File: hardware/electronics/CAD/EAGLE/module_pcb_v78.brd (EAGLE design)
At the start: 34.9 x 42.8 mm, 8 parts, among them J1 5557969-1

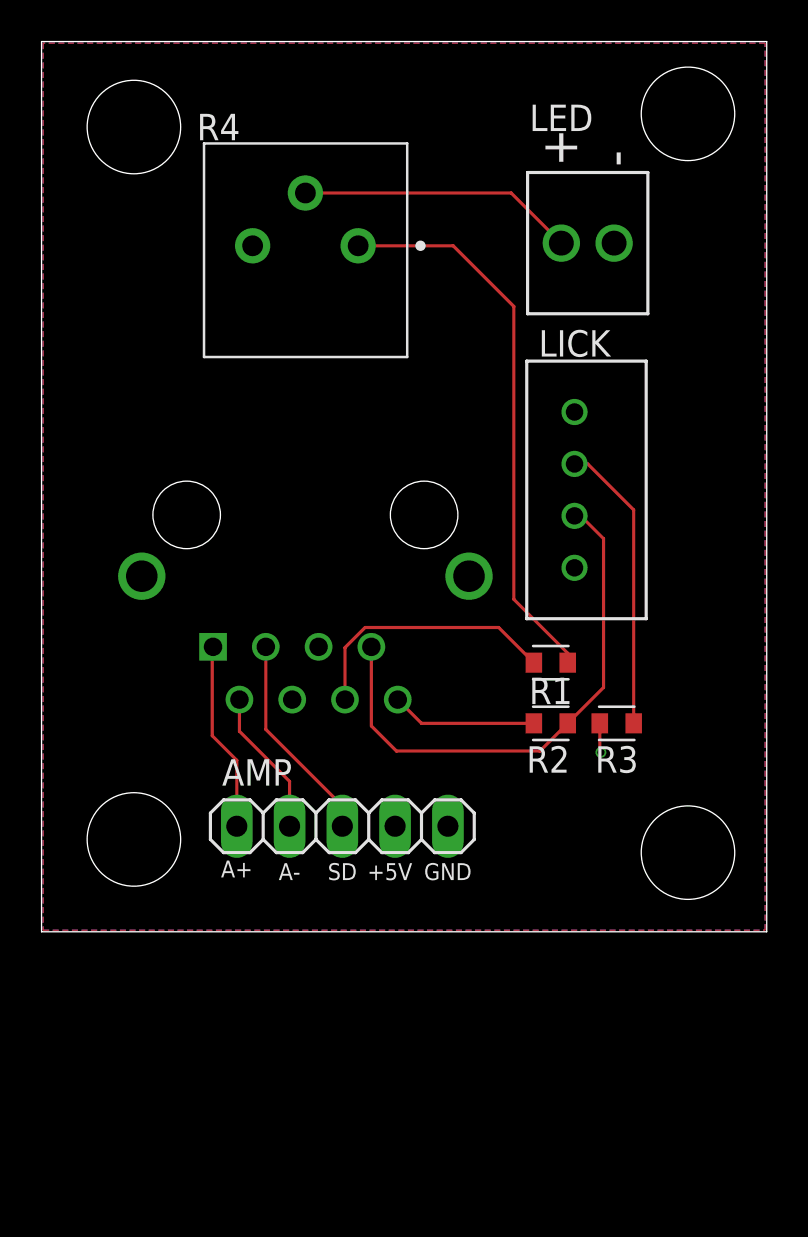
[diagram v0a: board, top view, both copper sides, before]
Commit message: round corners of module pcb
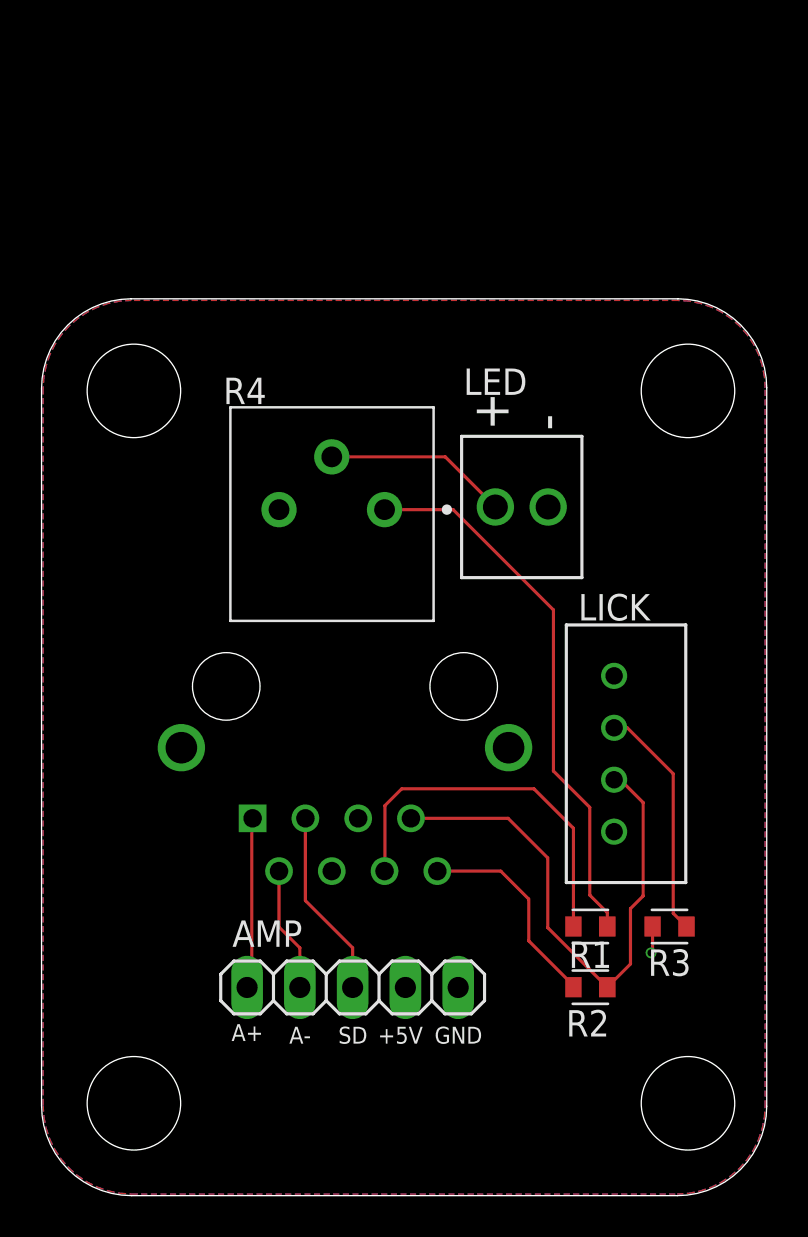
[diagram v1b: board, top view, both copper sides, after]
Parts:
- moved LED 13.1 mm to (24.4, 33.1)
- moved LICK 12.8 mm to (27.6, 25.0)
- moved R2 12.8 mm to (26.4, 10.0)
- moved R1 12.8 mm to (26.4, 13.0)
- moved R4 12.8 mm to (16.5, 33.0)
- moved R3 10.1 mm to (30.2, 13.0)
- moved J1 8.47 mm to (14.6, 24.5)
- moved AMP 7.78 mm to (15.0, 10.0)
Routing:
- net LED_ON: track 12.7 -> 18.1 mm
- net N$2: track 13.3 -> 8.87 mm
- net +3.3V: track 7.02 -> 10.1 mm
- net N$1: track 14.0 -> 11.4 mm
- net A-: track 7.10 -> 6.02 mm
- net SD: track 10.2 -> 9.08 mm
- net A+: track 9.14 -> 8.25 mm
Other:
- board size 34.9 x 42.8 mm -> 34.9 x 43.2 mm
